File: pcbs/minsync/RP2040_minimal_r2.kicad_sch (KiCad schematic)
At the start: 43 parts, among them J1 SWD_JST, J5 SWD_HEADERS, J6 Conn_01x01_Pin, J7 SSD1306, SW1 SW_Push, U1 NCP1117-3.3_SOT223, U2 W25Q128JVS, U3 RP2040, U4 Si5351A-B-GT, Y2 Crystal_GND24

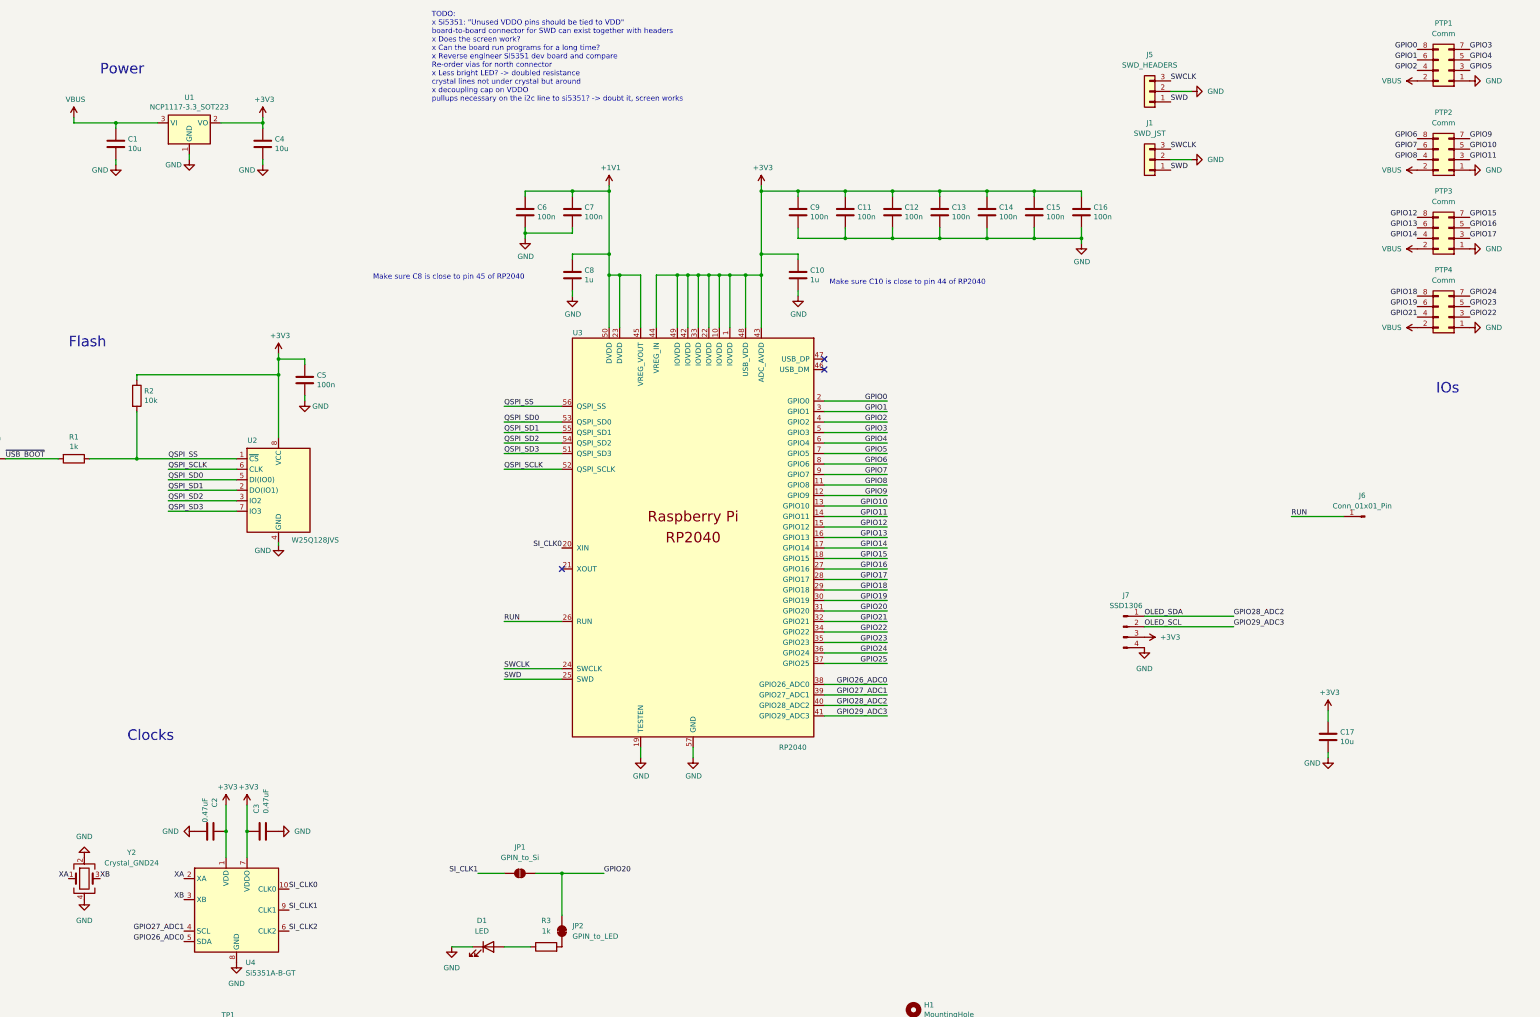
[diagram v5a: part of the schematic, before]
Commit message: minsync: Implement fixes for problems in v0.1, bump version to v0.2.
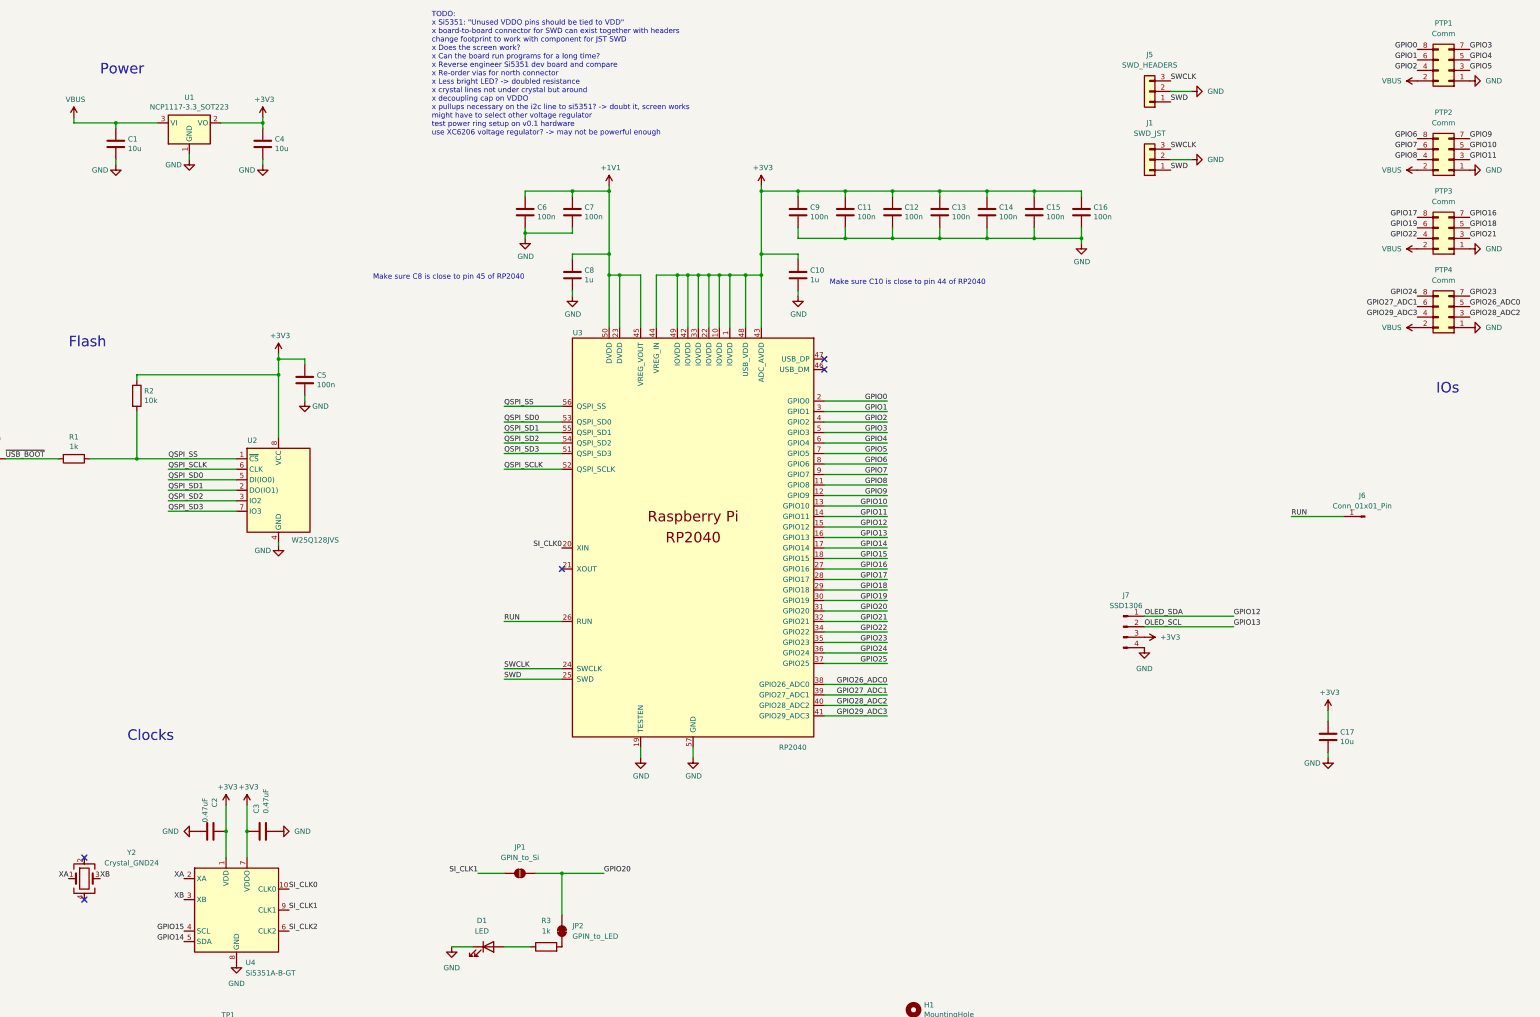
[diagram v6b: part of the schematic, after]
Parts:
- J1: footprint (none) -> Connector_JST:JST_ACH_BM03B-ACHSS-GAN-ETF_1x03-1MP_P1.20mm_Vertical; LCSC (none) -> C160389
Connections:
- net GND: no longer Y2.2, Y2.4
- net GPIO12: now also J7.1 (Pin_1); no longer PTP3.8 (Pin_8)
- net GPIO13: now also J7.2 (Pin_2); no longer PTP3.6 (Pin_6)
- net GPIO14: now also U4.5 (SDA); no longer PTP3.4 (Pin_4)
- net GPIO15: now also U4.4 (SCL); no longer PTP3.7 (Pin_7)
- net GPIO16: now also PTP3.7 (Pin_7); no longer PTP3.5 (Pin_5)
- net GPIO17: now also PTP3.8 (Pin_8); no longer PTP3.3 (Pin_3)
- net GPIO18: now also PTP3.5 (Pin_5); no longer PTP4.8 (Pin_8)
- net GPIO19: now also PTP3.6 (Pin_6); no longer PTP4.6 (Pin_6)
- net GPIO21: now also PTP3.3 (Pin_3); no longer PTP4.4 (Pin_4)
- net GPIO22: now also PTP3.4 (Pin_4); no longer PTP4.3 (Pin_3)
- net GPIO23: now also PTP4.7 (Pin_7); no longer PTP4.5 (Pin_5)
- net GPIO24: now also PTP4.8 (Pin_8); no longer PTP4.7 (Pin_7)
- net GPIO26_ADC0: now also PTP4.5 (Pin_5); no longer U4.5 (SDA)
- net GPIO27_ADC1: now also PTP4.6 (Pin_6); no longer U4.4 (SCL)
- net GPIO28_ADC2: now also PTP4.3 (Pin_3); no longer J7.1 (Pin_1)
- net GPIO29_ADC3: now also PTP4.4 (Pin_4); no longer J7.2 (Pin_2)
- no-connect marks 3 -> 5
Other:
- note added: "TODO: x Si5351: "Unused VDDO pins should be tied to VDD" x board-to-board connector for SWD can exist together with headers change footprint to work with component for JST SWD x Does the screen work? x Can the board run programs for a long time? x Reverse engineer Si5351 dev board and compare x Re-order vias for north connector x Less bright LED? -> doubled resistance x crystal lines not under cr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"
- note removed: "TODO: x Si5351: "Unused VDDO pins should be tied to VDD" board-to-board connector for SWD can exist together with headers x Does the screen work? x Can the board run programs for a long time? x Reverse engineer Si5351 dev board and compare Re-order vias for north connector x Less bright LED? -> doubled resistance crystal lines not under crystal but around x decoupling cap on VDDO pullups necessar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"
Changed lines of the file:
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@@
 	)
 	(no_connect
+		(at 50.8 222.25)
+	)
+	(no_connect
+		(at 50.8 232.41)
+	)
+	(no_connect
 		(at 166.37 152.4)
 	)
@@
 		)
 	)
-	(text "TODO:\nx Si5351: \"Unused VDDO pins should be tied to VDD\"\nboard-to-board connector for SWD can exist together with headers\nx Does the screen work?\nx Can the board run programs for a long time?\nx Reverse engineer Si5351 dev board and compare\nRe-order vias for north connector\nx Less bright LED? -> doubled resistance\ncrystal lines not under crystal but around\nx decoupling cap on VDDO\npullups necessary on the i2c line to si5351? -> doubt it, screen works"
+	(text "TODO:\nx Si5351: \"Unused VDDO pins should be tied to VDD\"\nx board-to-board connector for SWD can exist together with headers\nchange footprint to work with component for JST SWD\nx Does the screen work?\nx Can the board run programs for a long time?\nx Reverse engineer Si5351 dev board and compare\nx Re-order vias for north connector\nx Less bright LED? -> doubled resistance\nx crystal lines not under crystal but around\nx decoupling cap on VDDO\nx pullups necessary on the i2c line to si5351? -> doubt it, screen works\nmight have to select other voltage regulator\ntest power ring setup on v0.1 hardware\nuse XC6206 voltage regulator? -> may not be powerful enough"
 		(exclude_from_sim no)
 		(at 134.874 17.526 0)
@@
 	)
 	(label "GPIO24"
-		(at 386.08 86.36 0)
+		(at 373.38 86.36 180)
 		(fields_autoplaced yes)
 		(effects
@@
 				(size 1.27 1.27)
 			)
-			(justify left bottom)
+			(justify right bottom)
 		)
 	)
@@
 	)
 	(label "GPIO21"
-		(at 373.38 91.44 180)
+		(at 386.08 72.39 0)
 		(fields_autoplaced yes)
 		(effects
@@
 				(size 1.27 1.27)
 			)
-			(justify right bottom)
+			(justify left bottom)
 		)
 	)
@@
 	)
 	(label "GPIO17"
-		(at 386.08 72.39 0)
+		(at 373.38 67.31 180)
 		(fields_autoplaced yes)
 		(effects
@@
 				(size 1.27 1.27)
 			)
-			(justify left bottom)
+			(justify right bottom)
 		)
 	)
@@
 		)
 	)
+	(label "GPIO14"
+		(at 74.93 242.57 180)
+		(fields_autoplaced yes)
+		(effects
+			(font
+				(size 1.27 1.27)
+			)
+			(justify right bottom)
+		)
+	)
 	(label "GPIO10"
 		(at 245.11 137.16 180)
@@
 	)
 	(label "GPIO27_ADC1"
-		(at 74.93 240.03 180)
+		(at 373.38 88.9 180)
 		(fields_autoplaced yes)
 		(effects
@@
 	)
 	(label "GPIO12"
-		(at 373.38 67.31 180)
+		(at 328.93 163.83 0)
 		(fields_autoplaced yes)
 		(effects
@@
 				(size 1.27 1.27)
 			)
-			(justify right bottom)
+			(justify left bottom)
 		)
 	)
@@
 	)
 	(label "GPIO18"
-		(at 373.38 86.36 180)
+		(at 386.08 69.85 0)
 		(fields_autoplaced yes)
 		(effects
@@
 				(size 1.27 1.27)
 			)
-			(justify right bottom)
+			(justify left bottom)
 		)
 	)
@@
 	)
 	(label "GPIO28_ADC2"
-		(at 328.93 163.83 0)
+		(at 386.08 91.44 0)
 		(fields_autoplaced yes)
 		(effects
@@
 		)
 	)
+	(label "GPIO15"
+		(at 74.93 240.03 180)
+		(fields_autoplaced yes)
+		(effects
+			(font
+				(size 1.27 1.27)
+			)
+			(justify right bottom)
+		)
+	)
 	(label "GPIO20"
 		(at 176.53 226.06 0)
@@
 	)
 	(label "GPIO23"
-		(at 386.08 88.9 0)
+		(at 386.08 86.36 0)
 		(fields_autoplaced yes)
 		(effects
@@
 	)
 	(label "GPIO22"
-		(at 386.08 91.44 0)
-		(fields_autoplaced yes)
-		(effects
-			(font
-				(size 1.27 1.27)
-			)
-			(justify left bottom)
-		)
-	)
-	(label "GPIO15"
-		(at 386.08 67.31 0)
+		(at 373.38 72.39 180)
 		(fields_autoplaced yes)
 		(effects
@@
 				(size 1.27 1.27)
 			)
-			(justify left bottom)
+			(justify right bottom)
 		)
 	)
 	(label "GPIO16"
-		(at 386.08 69.85 0)
+		(at 386.08 67.31 0)
 		(fields_autoplaced yes)
 		(effects
@@
 	)
 	(label "GPIO26_ADC0"
-		(at 74.93 242.57 180)
+		(at 386.08 88.9 0)
 		(fields_autoplaced yes)
 		(effects
@@
 				(size 1.27 1.27)
 			)
-			(justify right bottom)
+			(justify left bottom)
 		)
 	)
 	(label "GPIO13"
-		(at 373.38 69.85 180)
+		(at 328.93 166.37 0)
 		(fields_autoplaced yes)
 		(effects
@@
 				(size 1.27 1.27)
 			)
-			(justify right bottom)
+			(justify left bottom)
 		)
 	)
 	(label "GPIO19"
-		(at 373.38 88.9 180)
+		(at 373.38 69.85 180)
 		(fields_autoplaced yes)
 		(effects
@@
 	)
 	(label "GPIO29_ADC3"
-		(at 328.93 166.37 0)
+		(at 373.38 91.44 180)
 		(fields_autoplaced yes)
 		(effects
@@
 				(size 1.27 1.27)
 			)
-			(justify left bottom)
+			(justify right bottom)
 		)
 	)
@@
 		)
 	)
-	(label "GPIO14"
-		(at 373.38 72.39 180)
-		(fields_autoplaced yes)
-		(effects
-			(font
-				(size 1.27 1.27)
-			)
-			(justify right bottom)
-		)
-	)
 	(symbol
 		(lib_id "MCU_RaspberryPi_RP2040:RP2040")
@@
 			)
 		)
-		(property "Footprint" ""
+		(property "Footprint" "Connector_JST:JST_ACH_BM03B-ACHSS-GAN-ETF_1x03-1MP_P1.20mm_Vertical"
 			(at 308.61 53.34 0)
 			(effects
@@
 			)
 		)
+		(property "LCSC" "C160389"
+			(at 308.61 53.34 0)
+			(effects
+				(font
+					(size 1.27 1.27)
+				)
+				(hide yes)
+			)
+		)
 		(pin "3"
 		)
@@
 	)
 	(symbol
-		(lib_name "GND_5")
-		(lib_id "power:GND")
-		(at 50.8 232.41 0)
-		(unit 1)
-		(exclude_from_sim no)
-		(in_bom yes)
-		(on_board yes)
-		(dnp no)
-		(fields_autoplaced yes)
-		(property "Reference" "#PWR046"
-			(at 50.8 238.76 0)
-			(effects
-				(font
-					(size 1.27 1.27)
-				)
-				(hide yes)
-			)
-		)
-		(property "Value" "GND"
-			(at 50.8 237.49 0)
-			(effects
-				(font
-					(size 1.27 1.27)
-				)
-			)
-		)
-		(property "Footprint" ""
-			(at 50.8 232.41 0)
-			(effects
-				(font
-					(size 1.27 1.27)
-				)
-				(hide yes)
-			)
-		)
-		(property "Datasheet" ""
-			(at 50.8 232.41 0)
-			(effects
-				(font
-					(size 1.27 1.27)
-				)
-				(hide yes)
-			)
-		)
-		(property "Description" "Power symbol creates a global label with name \"GND\" , ground"
-			(at 50.8 232.41 0)
-			(effects
-				(font
-					(size 1.27 1.27)
-				)
-				(hide yes)
-			)
-		)
-		(pin "1"
-		)
-		(instances
-			(project ""
-				(path "/8c0b3d8b-46d3-4173-ab1e-a61765f77d61"
-					(reference "#PWR046")
-					(unit 1)
-				)
-			)
-		)
-	)
-	(symbol
 		(lib_id "Jumper:SolderJumper_2_Open")
 		(at 156.21 226.06 0)
@@
 					(unit 1)
 				)
-			)
-		)
-	)
-	(symbol
-		(lib_name "GND_6")
-		(lib_id "power:GND")
-		(at 50.8 222.25 180)
-		(unit 1)
-		(exclude_from_sim no)
-		(in_bom yes)
-		(on_board yes)
-		(dnp no)
-		(fields_autoplaced yes)
-		(property "Reference" "#PWR047"
-			(at 50.8 215.9 0)
-			(effects
-				(font
-					(size 1.27 1.27)
-				)
-				(hide yes)
-			)
-		)
-		(property "Value" "GND"
-			(at 50.8 217.17 0)
-			(effects
-				(font
-					(size 1.27 1.27)
-				)
-			)
-		)
-		(property "Footprint" ""
-			(at 50.8 222.25 0)
-			(effects
-				(font
-					(size 1.27 1.27)
-				)
-				(hide yes)
-			)
-		)
-		(property "Datasheet" ""
-			(at 50.8 222.25 0)
-			(effects
-				(font
-					(size 1.27 1.27)
-				)
-				(hide yes)
-			)
-		)
-		(property "Description" "Power symbol creates a global label with name \"GND\" , ground"
-			(at 50.8 222.25 0)
-			(effects
-				(font
-					(size 1.27 1.27)
-				)
-				(hide yes)
-			)
-		)
-		(pin "1"
-		)
-		(instances
-			(project ""
-				(path "/8c0b3d8b-46d3-4173-ab1e-a61765f77d61"
-					(reference "#PWR047")
-					(unit 1)
-				)
